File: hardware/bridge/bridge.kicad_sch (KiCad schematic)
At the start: 58 parts, among them J1 XT30U-M, J2 Seg A, J3 Seg B, J4 Seg C, J5 Seg D, J6 Head, J7 OLED, J8 Shutdown button, J9 Ext 5V, Q1 NCE40P70K, U1 LMR51606XDBVR, U2 WeAct STM32G474 QFN48, U3 LSM6DSV16X breakout

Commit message: Bridge PCB: soft power switch, PA5 breakout, time-lag fuses
- Soft power switch: Q2 grounds the soft start's R1, so the button (J8,
  now BTN_A and BTN_B) or the bridge's PC4 hold turns the robot on. A
  stretch RC lets a tap last until the bridge has booted; Q3 gives PB5 an
  active-low button sense with no battery voltage on the pin; Q5 and Q4
  snap Q1 off in about 20 ms. Off leaves about 20 uA. JP2, open, bridges
  back to the old always-on behaviour.
- PA5 breakout pads (G 5V 3V3 A5) in the bottom-left corner, name block
  moved below them.
- Data-line zener footprints D4 to D7 dropped to make room; never fitted.
- Segment B and D feeds get a second via at their layer change; SEG C's
  feed runs round the board edge so it no longer walls off the bottom
  layer.
- Fuses changed to BHFUSE BSMD1206C time-lag parts: the Littelfuse 0458s
  were very fast-acting.
- JLC package, PDFs and 3D render regenerated; design note updated
  (docs/bridge-pcb.md section 6.5 has the firmware rules).
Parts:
- removed C8: 2.2u 50V, Capacitor_SMD:C_0805_2012Metric, symbol Device:C
- removed D4, D5, D6, D7: BZT52C5V6S, Diode_SMD:D_SOD-323, symbol Device:D_Zener
- removed J5: Seg D, Connector_JST:JST_PH_B3B-PH-K_1x03_P2.00mm_Vertical, symbol Connector_Generic:Conn_01x03
- removed J6: Head, Connector_JST:JST_PH_B4B-PH-K_1x04_P2.00mm_Vertical, symbol Connector_Generic:Conn_01x04
- removed L1: 33u, Inductor_SMD:L_Sunlord_SWPA4030S, symbol Device:L
- removed R11: 100k, Resistor_SMD:R_0603_1608Metric, symbol Device:R
- added C10: 100n 50V, Capacitor_SMD:C_0603_1608Metric, symbol Device:C
- added C14: 1u 50V, Capacitor_SMD:C_0603_1608Metric, symbol Device:C
- added D11: BAT54WS, Diode_SMD:D_SOD-323, symbol Device:D_Schottky
- added D12: 1N4148WS, Diode_SMD:D_SOD-323, symbol Device:D
- added D13: BZT52C12S, Diode_SMD:D_SOD-323, symbol Device:D_Zener
- added F5: 4A, Fuse:Fuse_1206_3216Metric, symbol Device:Fuse
- added J10: PA5 breakout, Connector_PinHeader_2.54mm:PinHeader_1x04_P2.54mm_Vertical, symbol Connector_Generic:Conn_01x04
- added J4: Seg C, Connector_JST:JST_PH_B3B-PH-K_1x03_P2.00mm_Vertical, symbol Connector_Generic:Conn_01x03
- added J8: Power button, Connector_JST:JST_PH_B2B-PH-K_1x02_P2.00mm_Vertical, symbol Connector_Generic:Conn_01x02
- added JP2: bridge = always on, Jumper:SolderJumper-2_P1.3mm_Open_RoundedPad1.0x1.5mm, symbol Jumper:SolderJumper_2_Open
- added Q2, Q3, Q5: 2N7002, Package_TO_SOT_SMD:SOT-23, symbol Transistor_FET:Q_NMOS_GSD
- added Q4: MMBT3906, Package_TO_SOT_SMD:SOT-23, symbol Transistor_BJT:Q_PNP_BEC
- added R10: 22k, Resistor_SMD:R_0603_1608Metric, symbol Device:R
- added R13, R15, R20, R22: 1M, Resistor_SMD:R_0603_1608Metric, symbol Device:R
- added R14: 470k, Resistor_SMD:R_0603_1608Metric, symbol Device:R
- added R21: 2.2M, Resistor_SMD:R_0603_1608Metric, symbol Device:R
- added R8: 0R, Resistor_SMD:R_0603_1608Metric, symbol Device:R
- C8: renamed from F6; value 1A -> 2.2u 50V; footprint Fuse:Fuse_1206_3216Metric -> Capacitor_SMD:C_0805_2012Metric; symbol Device:Fuse -> Device:C; LCSC C187559 -> C377773; MPN Littelfuse 0458001.DR -> (none)
- D9: renamed from J8; value Shutdown button -> BZT52C12S; footprint Connector_JST:JST_PH_B2B-PH-K_1x02_P2.00mm_Vertical -> Diode_SMD:D_SOD-323; symbol Connector_Generic:Conn_01x02 -> Device:D_Zener; LCSC (none) -> C19077447; MPN JST B2B-PH-K-S, through hole, fitted by hand -> (none); now in the parts list
- F1: LCSC C187564 -> C41367232; MPN Littelfuse 0458010.DR -> BHFUSE BSMD1206C-2100T, 10 A time lag, 32 V DC
- F2, F3, F4: LCSC C151127 -> C41367227; MPN Littelfuse 0458004.DR -> BHFUSE BSMD1206C-1400T, 4 A time lag, 72 V DC
- F6: renamed from F5; value 4A -> 1A; LCSC C151127 -> C41367221; MPN Littelfuse 0458004.DR -> BHFUSE BSMD1206C-1100T, 1 A time lag, 72 V DC
- J5: renamed from J4; value Seg C -> Seg D
- J6: renamed from R8; value 0R -> Head; footprint Resistor_SMD:R_0603_1608Metric -> Connector_JST:JST_PH_B4B-PH-K_1x04_P2.00mm_Vertical; symbol Device:R -> Connector_Generic:Conn_01x04; LCSC C21189 -> (none); MPN (none) -> JST B4B-PH-K-S, through hole, fitted by hand; now left out of the parts list
- L1: renamed from C10; value 100n 50V -> 33u; footprint Capacitor_SMD:C_0603_1608Metric -> Inductor_SMD:L_Sunlord_SWPA4030S; symbol Device:C -> Device:L; LCSC C14663 -> C83470; MPN (none) -> Sunlord SWPA4030S330MT
- R11: renamed from R10; value 22k -> 100k; LCSC C31850 -> C25803
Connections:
- net +3V3: now also J10.3 (Pin_3)
- net +5V: now also J10.2 (Pin_2)
- net 5V_BUCK: now also L1.2
- net BTN: now also Q3.3 (D); no longer D9.1 (Pin_1)
- net BUCK_FB: now also R10.1; no longer R11.1
- net BUCK_SW: now also L1.1
- net GND: now also C8.2, J6.2 (Pin_2), C10.2, C14.2, D13.2 (A), J10.1 (Pin_1), J4.3 (Pin_3), JP2.2 (B), Q2.2 (S), Q3.2 (S), Q5.2 (S), R10.2, R13.2, R15.2; no longer L1.2, R1.2, R11.2
- net LINK_RX: now also J6.4 (Pin_4)
- net LINK_TX: now also J6.3 (Pin_3)
- net Q1_G: now also Q4.3 (C)
- net SEG_C_C: now also J4.1 (Pin_1); no longer J5.1 (Pin_1)
- net SEG_D: now also R8.1; no longer J6.1
- net SEG_D_C: now also J5.1 (Pin_1), R8.2; no longer J6.2
- net VBAT_F: now also Q4.2 (E), R14.1, R22.2
- net VBAT_SENSE: now also R11.2
- net VBAT_SW: now also R11.1, C10.1, F5.1; no longer L1.1
- net VHEAD: now also F6.2, J6.1 (Pin_1); no longer C8.2
- net VSEG_C: now also J4.2 (Pin_2); no longer J5.2 (Pin_2)
- net VSEG_D: now also J5.2 (Pin_2), F5.2; no longer F6.2
- net PWR_HOLD: now reaches U2.36 (PC4)
- net PWR_HOLD: now also D11.2 (A)
- net PA5_IO: now reaches U2.37 (PA5)
- net PA5_IO: now also J10.4 (Pin_4)
- new net BTN_A: J8.1 (Pin_1), R14.2
- new net BTN_B: C14.1, D12.2 (A), D9.1 (K), J8.2 (Pin_2), Q3.1 (G), R15.1
- new net PWR_LO: JP2.1 (A), Q2.3 (D), R1.2, R20.1
- new net PWR_ON: D11.1 (K), D12.1 (K), Q2.1 (G), R13.1
- new net Q4_B: Q4.1 (B), R21.2, R22.1
- new net Q4_PULL: Q5.3 (D), R21.1
- new net Q5_G: D13.1 (K), Q5.1 (G), R20.2
- no-connect marks 28 -> 26
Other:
- note added: "Button or PC4 turns Q2 on, which grounds R1 and lets the soft start turn Q1 on. Q2 off: Q5 turns Q4 on, snapping Q1 off. JP2 bridged = always on, as before. Off leaves about 20 uA of leakage"
- note added: "Fuses time lag (BHFUSE BSMD1206C). Data lines: 0R links, room for a series resistor (hardware.md 5.6). PH 2.0 vertical through hole, hand fitted"
- note added: "J8 (button) joins BTN_A and BTN_B"
- note added: "PA5 breakout"
- note added: "Q3: PB5 reads low while the button is pressed"
- note added: "Soft power switch (docs/bridge-pcb.md 6.5)"
- note added: "Wire pads, bottom-left corner"
- note removed: "Fuses slow blow. Data lines: 0R fitted, 5.6 V zener not fitted (hardware.md 5.6). PH 2.0 vertical through hole, hand fitted"
- moved on the sheet: C8, F6, J5, R11

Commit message: Bridge PCB: head feed fuse F6 raised to 2 A
The head carrier's 5 V, 3 A buck draws about 0.85 A from a nearly flat
pack before amplifier peaks, too close to a 1 A rating. F6 is now the
BSMD1206C-1200T (C41367223), same 1206 footprint; fab outputs and the
schematic PDF regenerated, ERC clean.
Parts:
- F6: value 1A -> 2A; LCSC C41367221 -> C41367223; MPN BHFUSE BSMD1206C-1100T, 1 A time lag, 72 V DC -> BHFUSE BSMD1206C-1200T, 2 A time lag, 72 V DC
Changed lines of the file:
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@@
     (property "Reference" "F6" (at 228.6 87.63 90)
       (effects (font (size 1.27 1.27))))
-    (property "Value" "1A" (at 228.6 95.25 90)
+    (property "Value" "2A" (at 228.6 95.25 90)
       (effects (font (size 1.27 1.27))))
     (property "Footprint" "Fuse:Fuse_1206_3216Metric" (at 228.6 91.44 90)
@@
     (property "Description" "" (at 228.6 91.44 90)
       (effects (font (size 1.27 1.27)) (hide yes)))
-    (property "LCSC" "C41367221" (at 228.6 91.44 90)
+    (property "LCSC" "C41367223" (at 228.6 91.44 90)
       (effects (font (size 1.27 1.27)) (hide yes)))
-    (property "MPN" "BHFUSE BSMD1206C-1100T, 1 A time lag, 72 V DC" (at 228.6 91.44 90)
+    (property "MPN" "BHFUSE BSMD1206C-1200T, 2 A time lag, 72 V DC" (at 228.6 91.44 90)
       (effects (font (size 1.27 1.27)) (hide yes)))
     (pin "1")

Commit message: Bridge PCB rev B: WeAct header fix and pre-order review changes
- WeAct footprint: the VCC-side header (P1) had its rows swapped. The
  generator put odd pins on the inner row of both headers, but the two
  headers are the same part placed the same way round, so P1's odd pins
  are on its outer row (confirmed on the board: PB13 is on P1's inner
  row). Every P1 signal would have met its column neighbour.
- J7 (display) is now a 5-pin PH so the 4-pin head cable cannot go in it.
- C15, 1 uF X7R on PWR_ON: holds the power switch through a bridge reset
  and stretches a tap; C14 now X7R 0805, R14 220k.
- L1 SWPA6045S330MT (1.65 A saturation), D2 SMBJ26A (C19077580,
  Preferred).
- Buck column re-laid in current order; bulk capacitors stood on end
  under Q1; power capacitor ground pads solid; head feed VHEAD in a
  1.0 mm class.
- JP1 turned 180 degrees with hand-drawn links, and a top-layer keep-out
  across its cut line (no tracks, vias or pour).
- NYLON marked at H1 and H2 (segment C's feed runs under their heads).
- Routing tidied with tidy_head_pcb.py; DRC clean with schematic parity.
  JLC package, PDFs and render regenerated; design note section 6.6.
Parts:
- removed Q2, Q5: 2N7002, Package_TO_SOT_SMD:SOT-23, symbol Transistor_FET:Q_NMOS_GSD
- added C15: 1u 50V X7R, Capacitor_SMD:C_0805_2012Metric, symbol Device:C
- added JP2: bridge = always on, Jumper:SolderJumper-2_P1.3mm_Open_RoundedPad1.0x1.5mm, symbol Jumper:SolderJumper_2_Open
- added R21: 2.2M, Resistor_SMD:R_0603_1608Metric, symbol Device:R
- C14: value 1u 50V -> 1u 50V X7R; footprint Capacitor_SMD:C_0603_1608Metric -> Capacitor_SMD:C_0805_2012Metric; LCSC C15849 -> C28323
- D2: value SMBJ30A -> SMBJ26A; LCSC C19077584 -> C19077580
- J7: footprint Connector_JST:JST_PH_B4B-PH-K_1x04_P2.00mm_Vertical -> Connector_JST:JST_PH_B5B-PH-K_1x05_P2.00mm_Vertical; symbol Connector_Generic:Conn_01x04 -> Connector_Generic:Conn_01x05; MPN JST B4B-PH-K-S, through hole, fitted by hand -> JST B5B-PH-K-S, through hole, fitted by hand; 5 pins so the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
- L1: footprint Inductor_SMD:L_Sunlord_SWPA4030S -> Inductor_SMD:L_Sunlord_SWPA6045S; LCSC C83470 -> C83451; MPN Sunlord SWPA4030S330MT -> Sunlord SWPA6045S330MT
- Q2: renamed from JP2; value bridge = always on -> 2N7002; footprint Jumper:SolderJumper-2_P1.3mm_Open_RoundedPad1.0x1.5mm -> Package_TO_SOT_SMD:SOT-23; symbol Jumper:SolderJumper_2_Open -> Transistor_FET:Q_NMOS_GSD; LCSC (none) -> C8545; now in the parts list
- Q5: renamed from R21; value 2.2M -> 2N7002; footprint Resistor_SMD:R_0603_1608Metric -> Package_TO_SOT_SMD:SOT-23; symbol Device:R -> Transistor_FET:Q_NMOS_GSD; LCSC C22938 -> C8545
- R14: value 470k -> 220k; LCSC C23178 -> C22961
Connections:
- net GND: now also Q5.2 (S), C15.2, JP2.2 (B)
- net PWR_LO: now also Q2.3 (D), JP2.1 (A); no longer Q2.1 (A)
- net PWR_ON: now also Q2.1 (G), C15.1
- net Q4_B: now also R21.2; no longer Q5.2
- net Q4_PULL: now also Q5.3 (D), R21.1; no longer Q5.1
- net Q5_G: now also Q5.1 (G)
- no-connect marks 26 -> 27

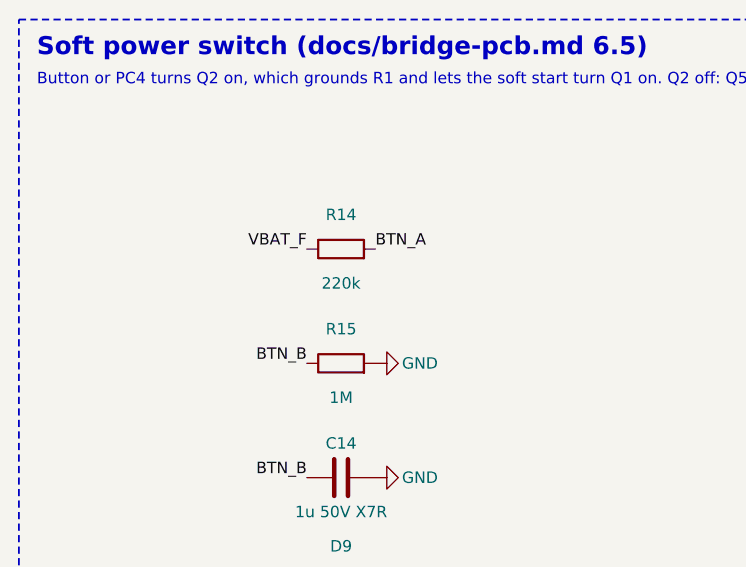
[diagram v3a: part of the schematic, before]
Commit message: Bridge PCB: second pre-order review fixes
- R14 220k to 100k (C25803, already on the board): a 70 ms tap latches
  at an 18 V pack with worst-case parts (220k needed about 150 ms).
- Buck feedback re-routed: from U1's FB pin straight to the bottom layer
  and down the west side to the divider, 17 mm, at least 1.9 mm from
  switch-node copper (it ran between the CB and SW pins and 0.22 mm
  beside L1's switch pad).
- Local copper: F3's segment B vias moved off its output pad; D2's
  ground pad solid with two stitching vias; 0.75 mm clearance round the
  XT30's + pad and a shorter ground bar beside it; JP2's ground pad on
  thermal spokes; a second via at two of VHEAD's layer changes.
- Silkscreen: J2's G above its own pin 3, clear of HEAD's B+; label
  strokes 0.15 mm; the IMU's VCC label clear of the pin-1 mark.
- Docs: the WeAct row rule in hardware/kicad/README.md, the head block
  diagram's UART direction, the carrier's exceptions in hardware.md 5.8,
  and corrected hold-up, tap and part-count figures in bridge-pcb.md.
- DRC clean with schematic parity; JLC package (30 BOM lines), PDFs and
  render regenerated.
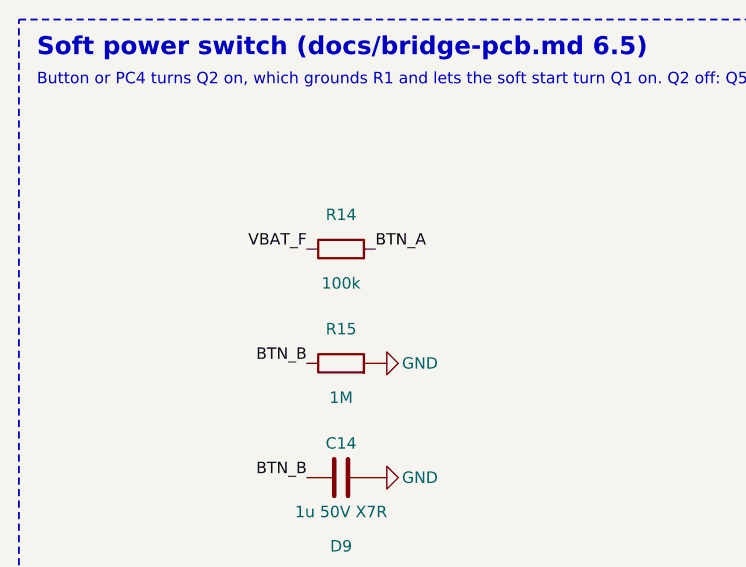
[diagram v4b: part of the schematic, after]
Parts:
- R14: value 220k -> 100k; LCSC C22961 -> C25803
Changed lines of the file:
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@@
     (property "Reference" "R14" (at 50.8 313.69 90)
       (effects (font (size 1.27 1.27))))
-    (property "Value" "220k" (at 50.8 321.31 90)
+    (property "Value" "100k" (at 50.8 321.31 90)
       (effects (font (size 1.27 1.27))))
     (property "Footprint" "Resistor_SMD:R_0603_1608Metric" (at 50.8 317.5 90)
@@
     (property "Description" "" (at 50.8 317.5 90)
       (effects (font (size 1.27 1.27)) (hide yes)))
-    (property "LCSC" "C22961" (at 50.8 317.5 90)
+    (property "LCSC" "C25803" (at 50.8 317.5 90)
       (effects (font (size 1.27 1.27)) (hide yes)))
     (pin "1")
